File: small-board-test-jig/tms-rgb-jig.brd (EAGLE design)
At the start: 91.2 x 28.7 mm, 15 parts, among them J10 R, J11 G, J12 B, J13 S_75, J14 GND, J15 S_TTL, J16 PIN1, J4 R-Y, J5 B-Y, J6 Y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

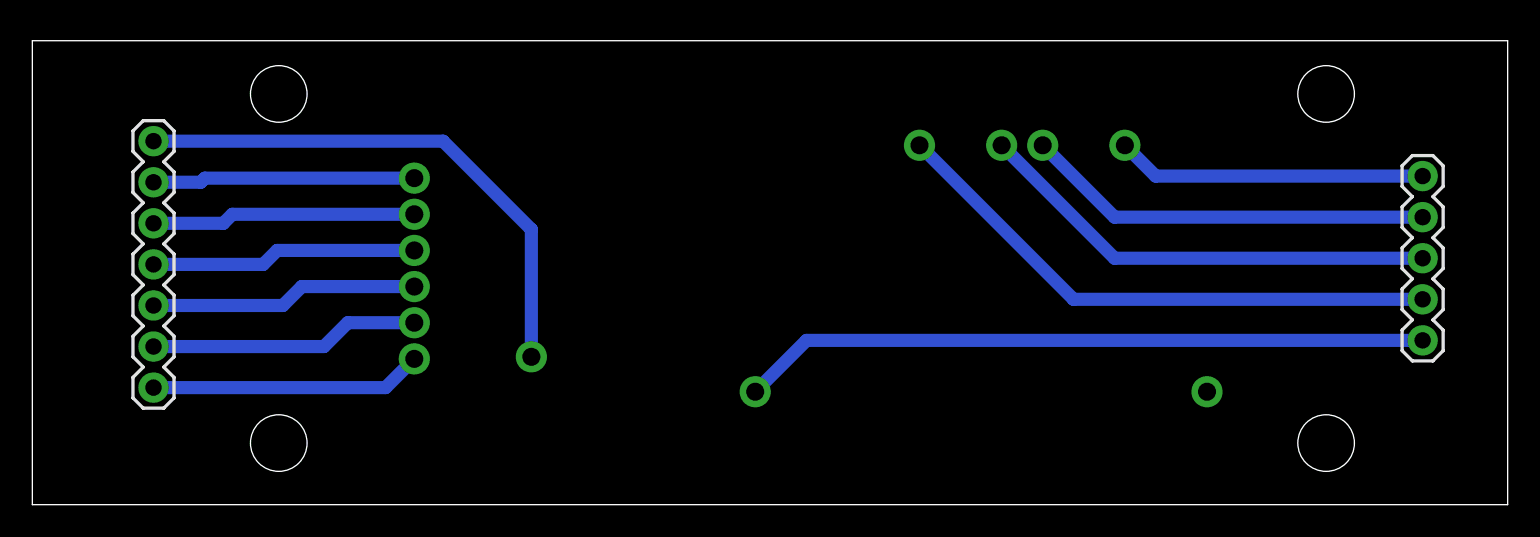
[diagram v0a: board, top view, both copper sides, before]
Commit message: Update jig for v2
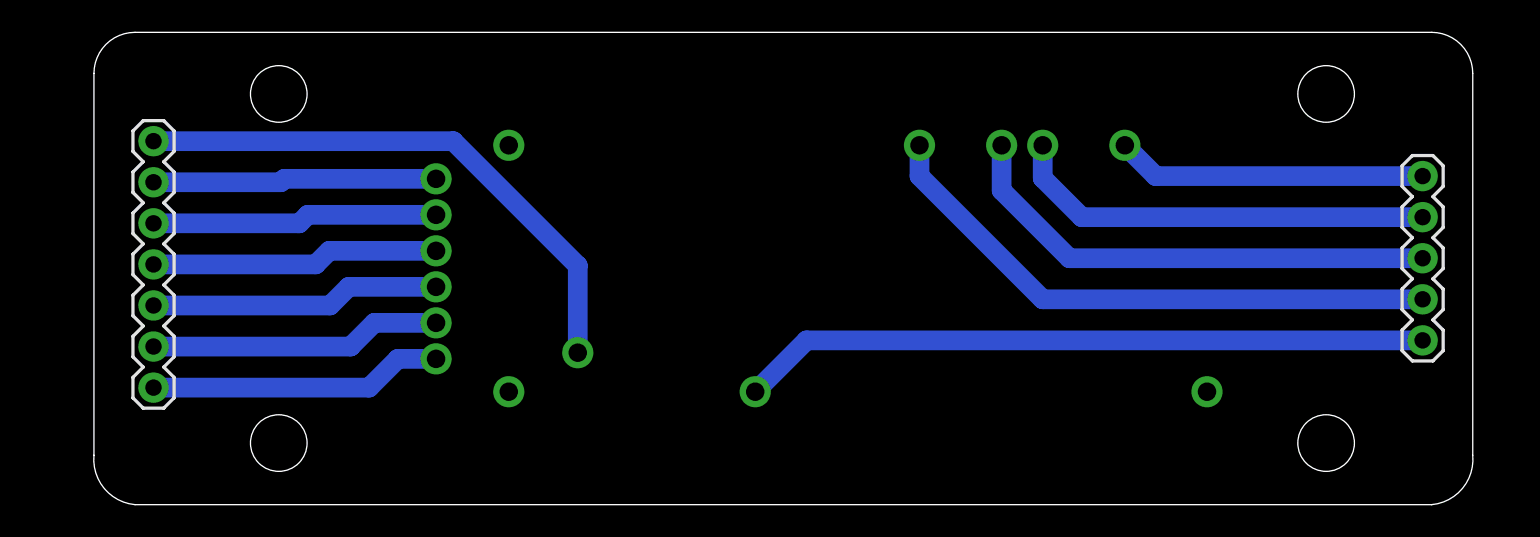
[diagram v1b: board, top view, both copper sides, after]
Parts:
- added J17: PIN18, tms-rgb-jig:POGO
- added J18: PIN23, tms-rgb-jig:POGO
- J13: value S_75 -> S75
- J15: value S_TTL -> TTL
- J2: value (none) -> CONN_07
- J3: value (none) -> CONN_05
- moved J15 2.88 mm to (33.7, 9.40)
- moved J14 1.35 mm to (25.0, 20.2)
- moved J13 1.35 mm to (25.0, 17.9)
- moved J12 1.35 mm to (25.0, 15.7)
- moved J11 1.35 mm to (25.0, 13.5)
- moved J10 1.35 mm to (25.0, 11.2)
- moved J9 1.35 mm to (25.0, 9.02)
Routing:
- net N$3: track 28.9 -> 30.6 mm
- net N$6: track 16.9 -> 18.2 mm
- net N$7: track 16.7 -> 18.1 mm
- net N$8: track 16.6 -> 18.0 mm
- net N$9: track 16.5 -> 17.8 mm
- net N$10: track 16.4 -> 17.7 mm
- net N$11: track 16.2 -> 17.6 mm
- net N$12: track 33.5 -> 34.8 mm
- net N$2: track 25.3 -> 26.5 mm
- net N$4: track 35.1 -> 36.2 mm
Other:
- board size 91.2 x 28.7 mm -> 85.3 x 29.2 mm
- board text added: "TMS-RGB Jig 2020 v2 @npiegdon"
- board text removed: "TMS-RGB Jig 2020 v1 @npiegdon"
